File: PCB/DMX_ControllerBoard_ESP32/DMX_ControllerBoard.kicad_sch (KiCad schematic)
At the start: 41 parts, among them J1 Screw_Terminal_01x03, J2 Screw_Terminal_01x03, J3 PWR_IN, J4 Screw_Terminal_01x03, J5 Conn_Left, J6 Screw_Terminal_01x03, J7 ProgrammingHeader, SW1 SW_SPST, SW2 SW_SPST, SW3 SW_SPST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

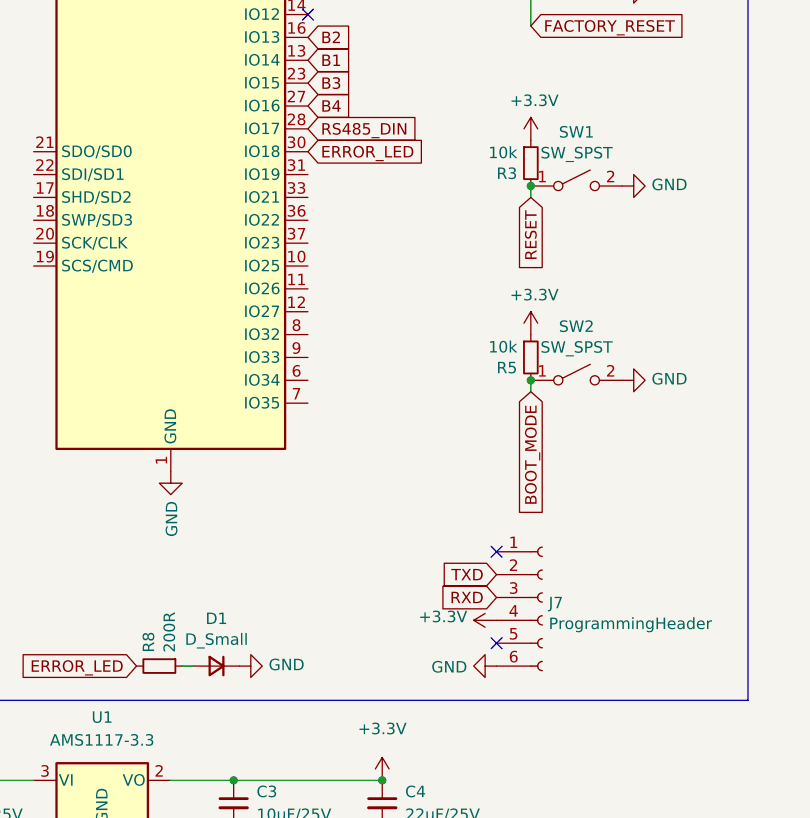
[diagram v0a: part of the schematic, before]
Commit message: Added more labeling to ESP32 board
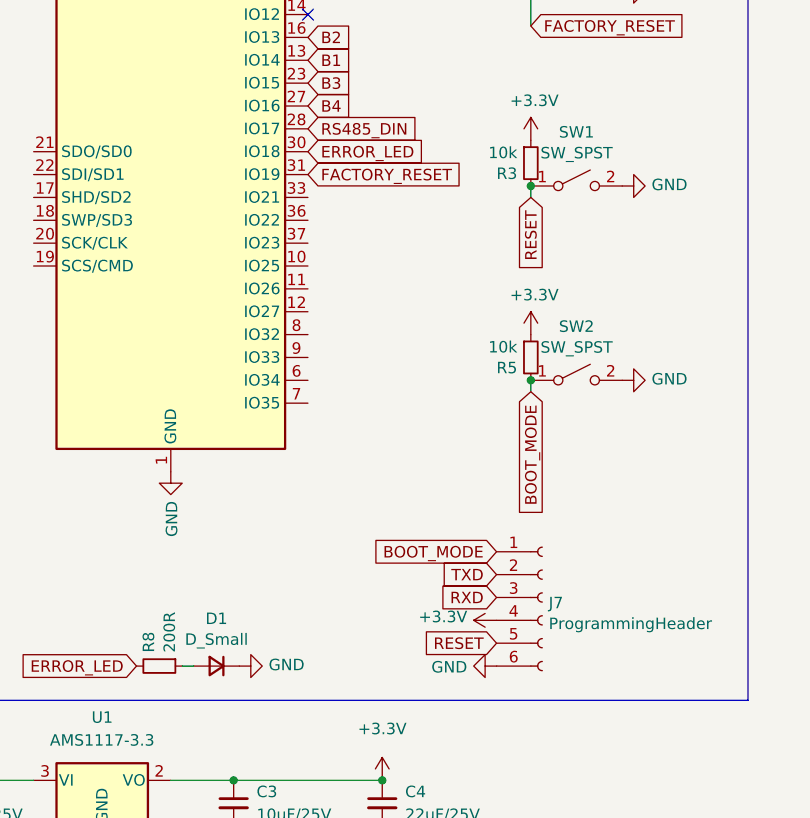
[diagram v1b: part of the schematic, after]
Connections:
- net BOOT_MODE: now also J7.1 (Pin_1)
- net FACTORY_RESET: now also U3.31 (IO19)
- net RESET: now also J7.5 (Pin_5)
- no-connect marks 10 -> 8
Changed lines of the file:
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@@
   (no_connect (at 130.81 29.21))
   (no_connect (at 61.595 53.34))
-  (no_connect (at 82.55 118.11))
-  (no_connect (at 82.55 128.27))
   (wire (pts (xy 156.21 31.75) (xy 156.21 26.67))
     (stroke (width 0) (type default) (color 0 0 0 0))
@@
     )
   )
+  (global_label "BOOT_MODE" (shape input) (at 82.55 118.11 180) (fields_autoplaced)
+    (effects (font (size 1.27 1.27)) (justify right))
+    (property "Intersheet References" "${INTERSHEET_REFS}" (id 0) (at 142.24 156.21 0)
+      (effects (font (size 1.27 1.27)) hide)
+    )
+  )
   (global_label "B1" (shape input) (at 61.595 63.5 0) (fields_autoplaced)
     (effects (font (size 1.27 1.27)) (justify left))
@@
     )
   )
+  (global_label "FACTORY_RESET" (shape input) (at 61.595 76.2 0) (fields_autoplaced)
+    (effects (font (size 1.27 1.27)) (justify left))
+    (property "Intersheet References" "${INTERSHEET_REFS}" (id 0) (at -24.765 16.51 0)
+      (effects (font (size 1.27 1.27)) hide)
+    )
+  )
   (global_label "B3" (shape input) (at 257.81 46.99 180) (fields_autoplaced)
     (effects (font (size 1.27 1.27)) (justify right))
     (property "Intersheet References" "${INTERSHEET_REFS}" (id 0) (at 0 0 0)
+      (effects (font (size 1.27 1.27)) hide)
+    )
+  )
+  (global_label "RESET" (shape input) (at 82.55 128.27 180) (fields_autoplaced)
+    (effects (font (size 1.27 1.27)) (justify right))
+    (property "Intersheet References" "${INTERSHEET_REFS}" (id 0) (at 53.34 90.17 0)
       (effects (font (size 1.27 1.27)) hide)
     )
@@
   (symbol (lib_id "power:PWR_FLAG") (at 21.59 173.99 0) (unit 1)
     (in_bom yes) (on_board yes)
-    (property "Reference" "" (id 0) (at 21.59 172.085 0)
+    (property "Reference" "#FLG0102" (id 0) (at 21.59 172.085 0)
       (effects (font (size 1.27 1.27)) hide)
     )
@@
   (symbol (lib_id "power:PWR_FLAG") (at 21.59 176.53 180) (unit 1)
     (in_bom yes) (on_board yes)
-    (property "Reference" "" (id 0) (at 21.59 178.435 0)
+    (property "Reference" "#FLG0103" (id 0) (at 21.59 178.435 0)
       (effects (font (size 1.27 1.27)) hide)
     )
@@
   (symbol (lib_id "power:PWR_FLAG") (at 91.44 168.91 0) (unit 1)
     (in_bom yes) (on_board yes)
-    (property "Reference" "" (id 0) (at 91.44 167.005 0)
-      (effects (font (size 1.27 1.27)) hide)
-    )
+    (property "Reference" "#FLG0101" (id 0) (at 91.44 167.005 0)
+      (effects (font (size 1.27 1.27)) hide)
+    )

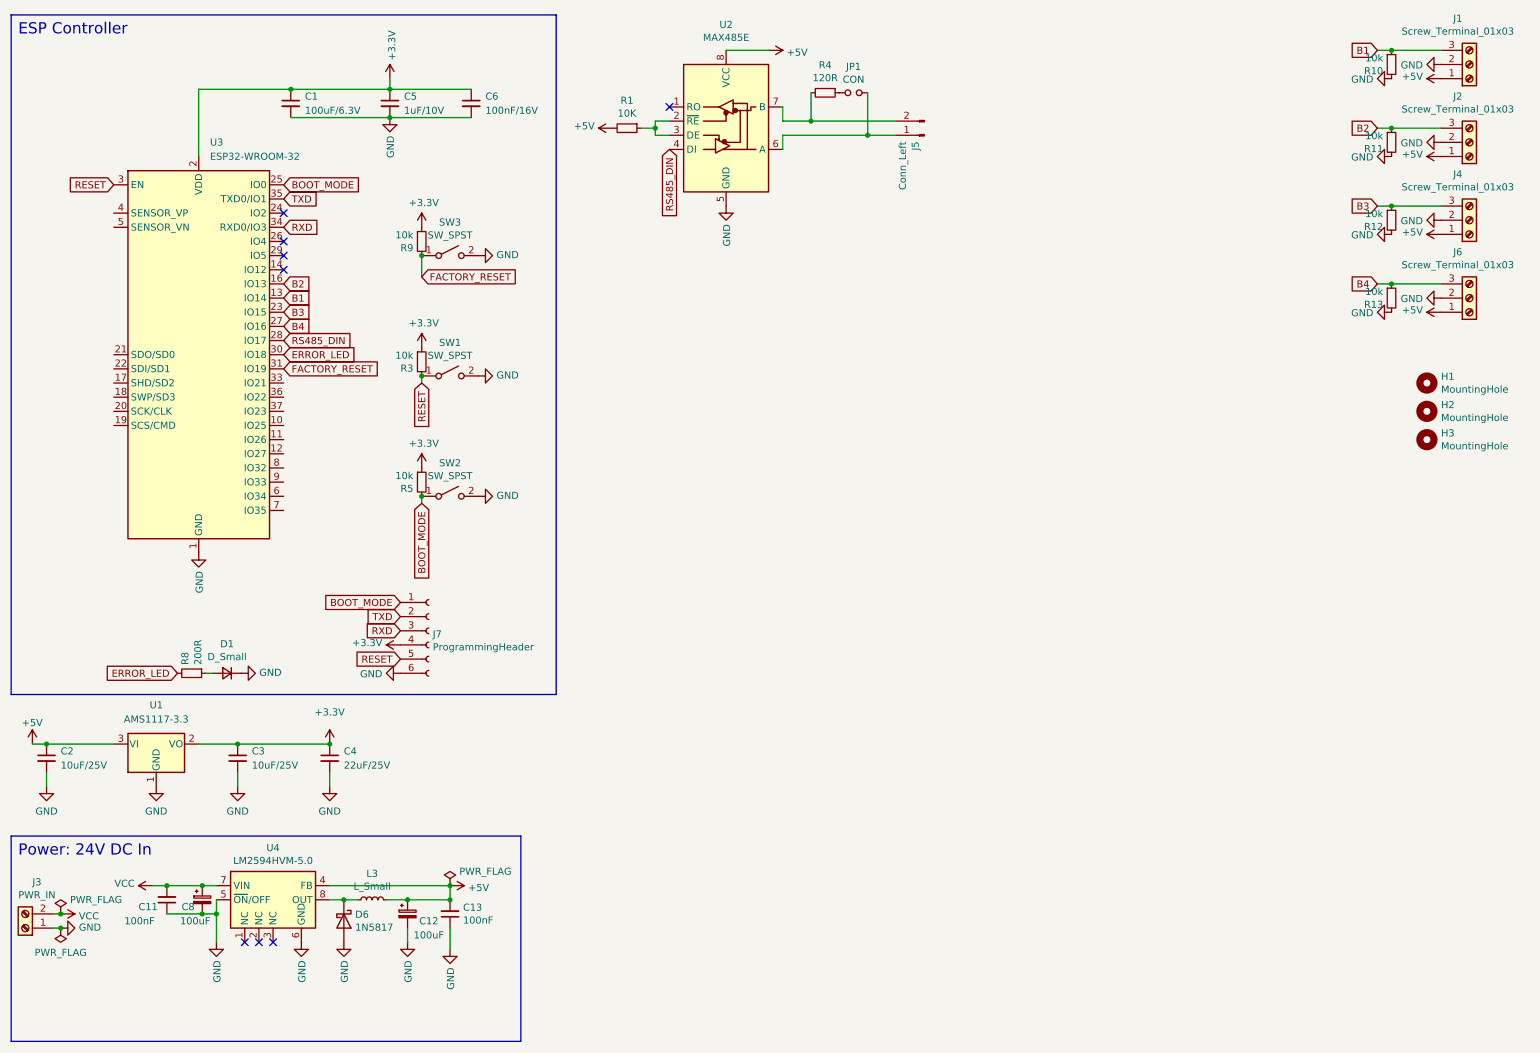
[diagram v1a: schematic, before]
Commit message: Initial commit of ESP32 based PCB
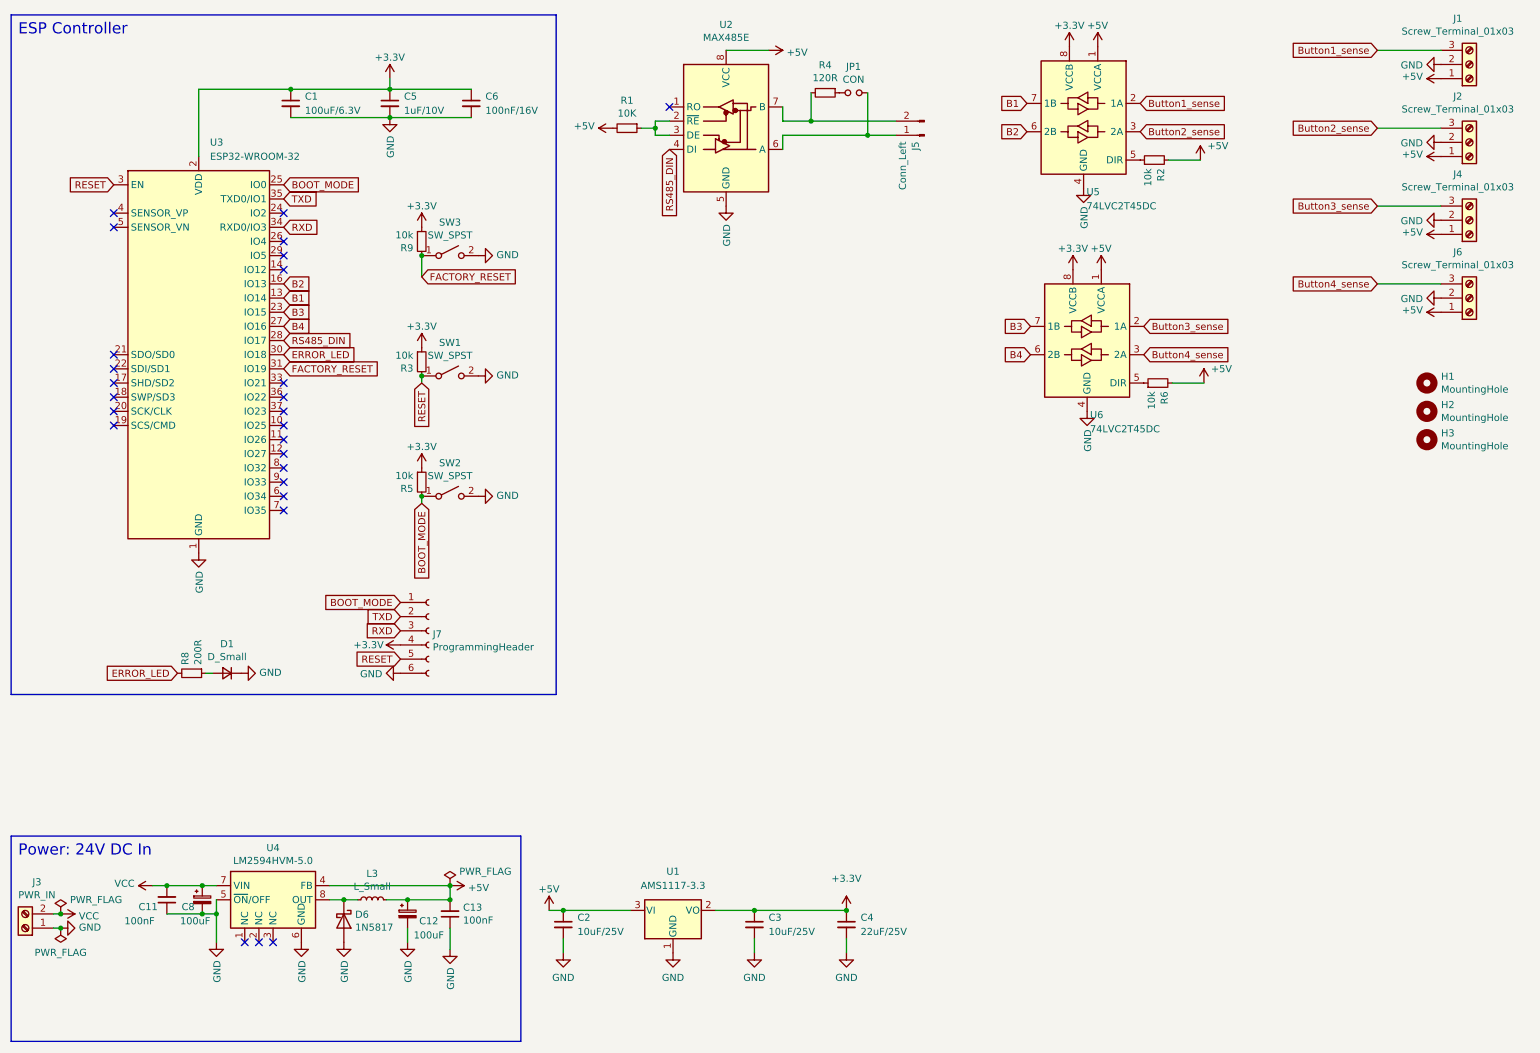
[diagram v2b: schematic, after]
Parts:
- removed R10, R11, R12, R13: 10k, Resistor_SMD:R_0805_2012Metric_Pad1.20x1.40mm_HandSolder, symbol Device:R_Small
- added R2, R6: 10k, Resistor_SMD:R_0805_2012Metric_Pad1.20x1.40mm_HandSolder, symbol Device:R_Small
- added U5, U6: 74LVC2T45DC, Package_SO:VSSOP-8_2.3x2mm_P0.5mm, symbol Logic_LevelTranslator:74LVC2T45DC
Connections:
- net +5V: now also R2.2, R6.2, U5.1 (VCCA), U6.1 (VCCA)
- net B1: now also U5.7 (1B); no longer J1.3 (Pin_3)
- net B2: now also U5.6 (2B); no longer J2.3 (Pin_3)
- net B3: now also U6.7 (1B); no longer J4.3 (Pin_3)
- net B4: now also U6.6 (2B); no longer J6.3 (Pin_3)
- net GND: now also U5.4 (GND), U6.4 (GND)
- net +3V3 renamed +3.3V
- net +3.3V: now also U5.8 (VCCB), U6.8 (VCCB)
- new net: R6.1, U6.5 (DIR)
- new net: R2.1, U5.5 (DIR)
- new net Button1_sense: J1.3 (Pin_3), U5.2 (1A)
- new net Button2_sense: J2.3 (Pin_3), U5.3 (2A)
- new net Button3_sense: J4.3 (Pin_3), U6.2 (1A)
- new net Button4_sense: J6.3 (Pin_3), U6.3 (2A)
- no-connect marks 8 -> 26
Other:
- moved on the sheet: C2, C3, C4, U1
